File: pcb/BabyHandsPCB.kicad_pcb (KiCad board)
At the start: 2 copper layers, 44 parts

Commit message: Route matrix
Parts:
- removed Dn: D_Small, kbd:D3_TH_SMD
- added D10: D_Small, kbd:D3_TH_SMD, F.Cu at (108.0, 192.1)
- MX1, MX10, MX11, MX12, MX13, MX14, MX15, MX16, MX17, MX19, MX2, MX20, MX21, MX3, MX4, MX5, MX6, MX7, MX8, MX9: footprint kbd:MX_ALPS_PG1350_noLed -> kbd:CherryMX_Choc_Hotswap
- MX18, MX22: footprint kbd:MX_ALPS_PG1350_noLed_1.75u -> kbd:CherryMX_Choc_Hotswap_1.5u
- moved MX10 125.7 mm to (117.7, 194.7)
- moved D18 125.0 mm to (166.7, 202.4), turned to 320 degrees
- moved D22 124.4 mm to (180.4, 213.2), turned to 320 degrees
- moved MX18 123.9 mm to (173.8, 193.7), turned to 320 degrees
- moved MX22 123.2 mm to (188.1, 205.6), turned to 320 degrees
- moved MX14 122.7 mm to (145.3, 196.1)
- moved MX17 121.7 mm to (123.0, 167.5)
- moved D14 121.2 mm to (135.8, 190.6)
- moved D17 121.1 mm to (112.7, 167.5)
- moved MX21 118.1 mm to (145.3, 167.5)
- moved MX16 117.8 mm to (123.0, 145.3)
- moved D21 117.4 mm to (134.9, 167.5)
- moved D16 117.3 mm to (112.7, 145.3)
- moved MX20 114.3 mm to (145.3, 145.3)
- moved MX15 114.0 mm to (123.0, 123.0)
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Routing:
- net Col5: track 0.00 -> 243.6 mm, vias 0 -> 9
- net Col3: track 0.00 -> 240.0 mm, vias 0 -> 9
- net Col2: track 0.00 -> 223.0 mm, vias 0 -> 9
- net Col4: track 0.00 -> 212.8 mm, vias 0 -> 8
- net Row1: track 0.00 -> 186.1 mm
- net Row2: track 0.00 -> 183.3 mm
- net Col1: track 0.00 -> 142.9 mm, vias 0 -> 7
- net Row0: track 44.7 -> 184.2 mm
- net Col0: track 0.00 -> 134.2 mm, vias 0 -> 7
- net Row3: track 0.00 -> 99.3 mm
- net Net-(D2-Pad2): track 0.00 -> 55.3 mm, vias 0 -> 2
- net Net-(D14-Pad2): track 0.00 -> 53.6 mm, vias 0 -> 2
- net Net-(D17-Pad2): track 0.00 -> 51.5 mm, vias 0 -> 2
- net Net-(D11-Pad2): track 0.00 -> 51.0 mm, vias 0 -> 2
- net Net-(D21-Pad2): track 0.00 -> 49.8 mm, vias 0 -> 2
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
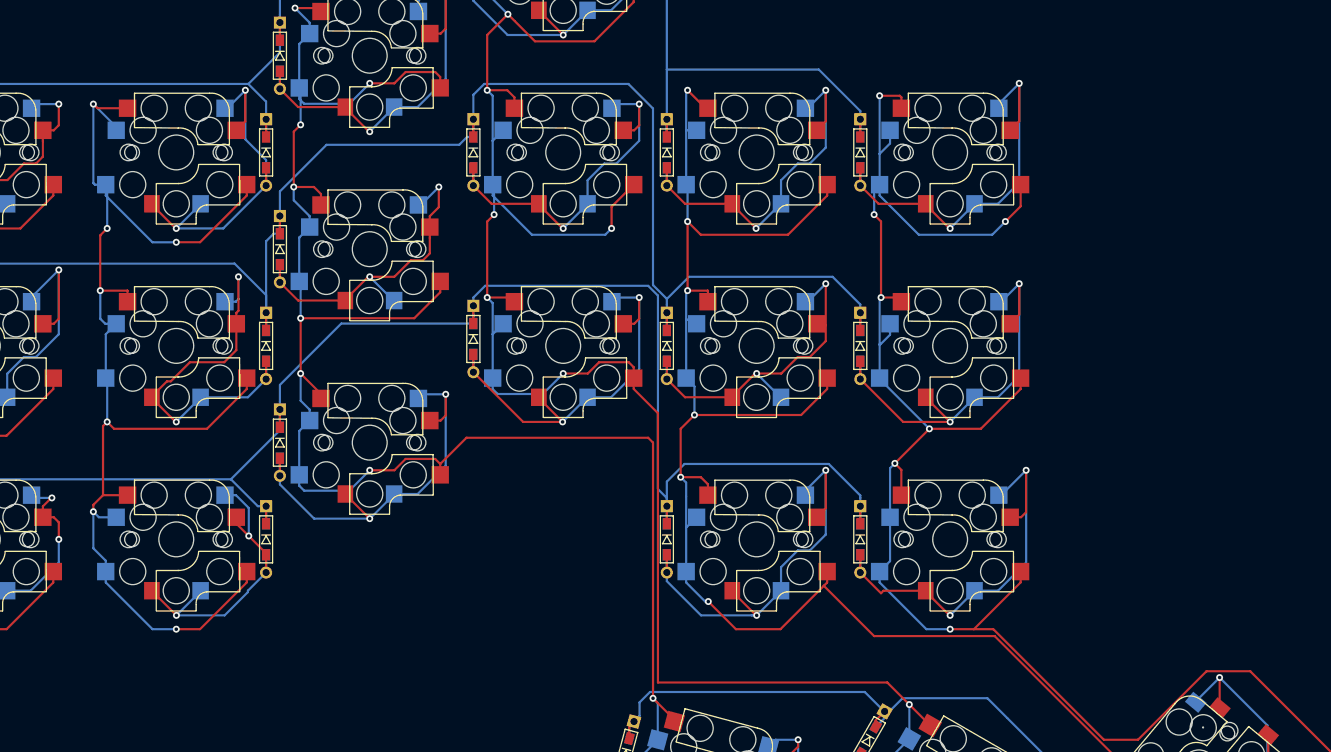
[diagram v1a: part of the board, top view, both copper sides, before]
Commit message: Add pro micro
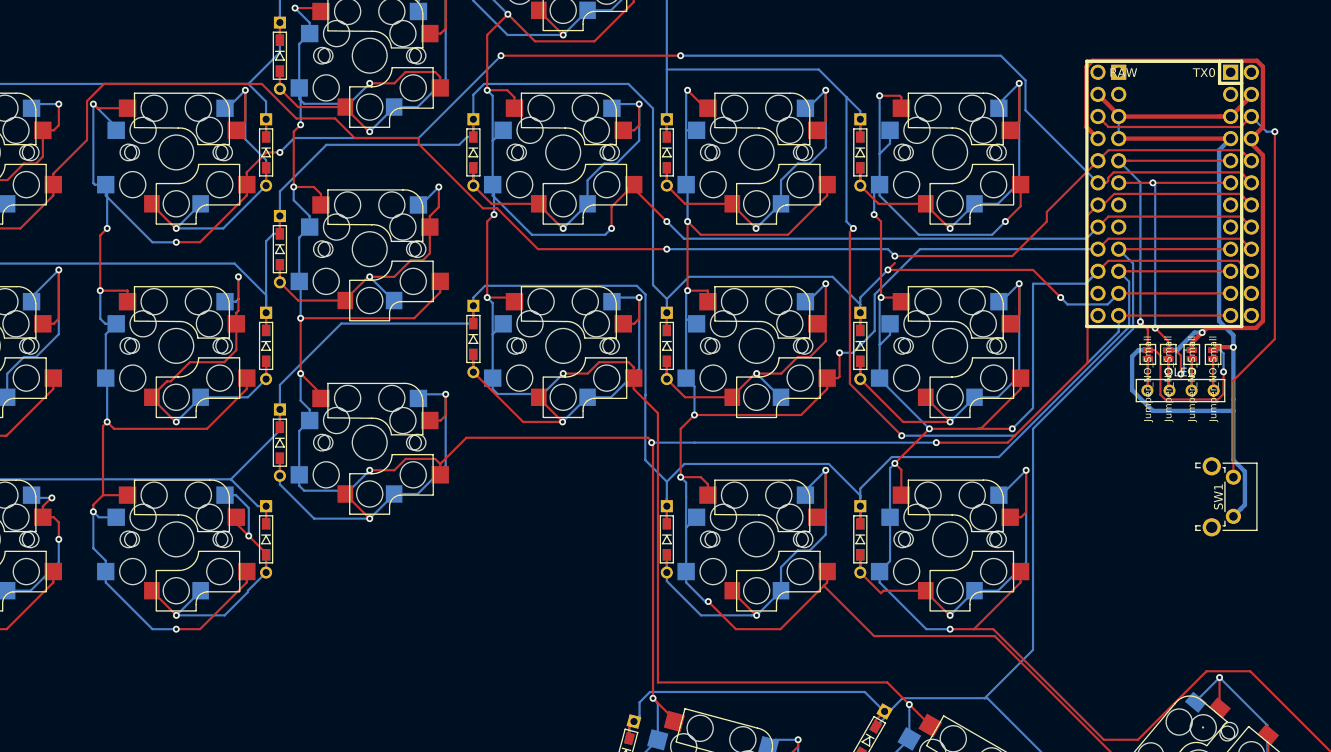
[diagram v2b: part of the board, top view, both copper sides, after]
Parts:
- added J1: Conn_01x04, kbd:OLED, F.Cu at (167.9, 150.4)
- added JP1: Jumper_NO_Small, kbd:Jumper, F.Cu at (175.5, 146.2)
- added JP2: Jumper_NO_Small, kbd:Jumper, F.Cu at (173.0, 146.2)
- added JP3: Jumper_NO_Small, kbd:Jumper, F.Cu at (170.3, 146.2)
- added JP4: Jumper_NO_Small, kbd:Jumper, F.Cu at (168.0, 146.2)
- added JP5: Jumper_NO_Small, kbd:Jumper, B.Cu at (175.5, 146.2)
- added JP6: Jumper_NO_Small, kbd:Jumper, B.Cu at (173.0, 146.2)
- added JP7: Jumper_NO_Small, kbd:Jumper, B.Cu at (170.3, 146.2)
- added JP8: Jumper_NO_Small, kbd:Jumper, B.Cu at (168.0, 146.2)
- added SW1: SW_PUSH, Button_Switch_THT:SW_Tactile_SPST_Angled_PTS645Vx31-2LFS, F.Cu at (177.8, 160.3)
- added U1: ProMicro, Keebio-Parts:ArduinoProMicro-BackSide, B.Cu at (169.9, 127.8)
- added U2: ProMicro, Keebio-Parts:ArduinoProMicro-BackSide, F.Cu at (172.2, 127.8)
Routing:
- net Col0: track 134.2 -> 294.8 mm, vias 7 -> 9
- net Col1: track 142.9 -> 274.5 mm, vias 7 -> 10
- net GND: track 0.00 -> 102.1 mm, vias 0 -> 1
- net Col2: track 223.0 -> 314.2 mm, vias 9 -> 11
- net Row0: track 184.2 -> 270.6 mm, vias 0 -> 2
- net Col3: track 240.0 -> 315.3 mm, vias 9 -> 10
- net VCC: track 0.00 -> 75.0 mm, vias 0 -> 1
- net Row3: track 99.3 -> 171.5 mm
- net RST: track 0.00 -> 63.7 mm, vias 0 -> 1
- net Col4: track 212.8 -> 272.7 mm, vias 8 -> 9
- net Row2: track 183.3 -> 240.0 mm
- net SDA: track 0.00 -> 56.0 mm, vias 0 -> 2
- net Col5: track 243.6 -> 294.0 mm, vias 9 -> 10
- net Row1: track 186.1 -> 234.1 mm, vias 0 -> 2
- net SCL: track 0.00 -> 40.5 mm, vias 0 -> 3
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
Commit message: Add outline
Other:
- board outline added: 186.5 x 136.7 mm
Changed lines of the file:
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@@
   (general
     (thickness 1.6)
-    (drawings 0)
+    (drawings 14)
     (tracks 1231)
     (zones 0)
@@
     )
   )
+  (gr_line (start 65.866 99.288) (end 65.866 110.288) (layer Edge.Cuts) (width 0.05))
+  (gr_line (start 88.316 99.288) (end 65.866 99.288) (layer Edge.Cuts) (width 0.05))
+  (gr_line (start 88.316 88.088) (end 88.316 99.288) (layer Edge.Cuts) (width 0.05))
+  (gr_line (start 114.166 88.088) (end 88.316 88.088) (layer Edge.Cuts) (width 0.05))
+  (gr_line (start 114.166 110.938) (end 114.166 88.088) (layer Edge.Cuts) (width 0.05))
+  (gr_line (start 185.166 110.938) (end 114.166 110.938) (layer Edge.Cuts) (width 0.05))
+  (gr_line (start 21.316 179.788) (end 21.316 110.288) (layer Edge.Cuts) (width 0.05))
+  (gr_line (start 67.416 179.788) (end 21.316 179.788) (layer Edge.Cuts) (width 0.05))
+  (gr_line (start 103.516 204.838) (end 67.416 179.788) (layer Edge.Cuts) (width 0.05))
+  (gr_line (start 187.066 224.788) (end 103.516 204.838) (layer Edge.Cuts) (width 0.05))
+  (gr_line (start 207.816 200.588) (end 187.066 224.788) (layer Edge.Cuts) (width 0.05))
+  (gr_line (start 185.116 182.088) (end 207.816 200.588) (layer Edge.Cuts) (width 0.05))
+  (gr_line (start 185.166 110.938) (end 185.116 182.088) (layer Edge.Cuts) (width 0.05))
+  (gr_line (start 21.316 110.288) (end 65.866 110.288) (layer Edge.Cuts) (width 0.05))
   (segment (start 25.9025 128.93125) (end 31.33125 128.93125) (width 0.25) (layer F.Cu) (net 1))
   (segment (start 23.8125 126.84125) (end 25.9025 128.93125) (width 0.25) (layer F.Cu) (net 1))

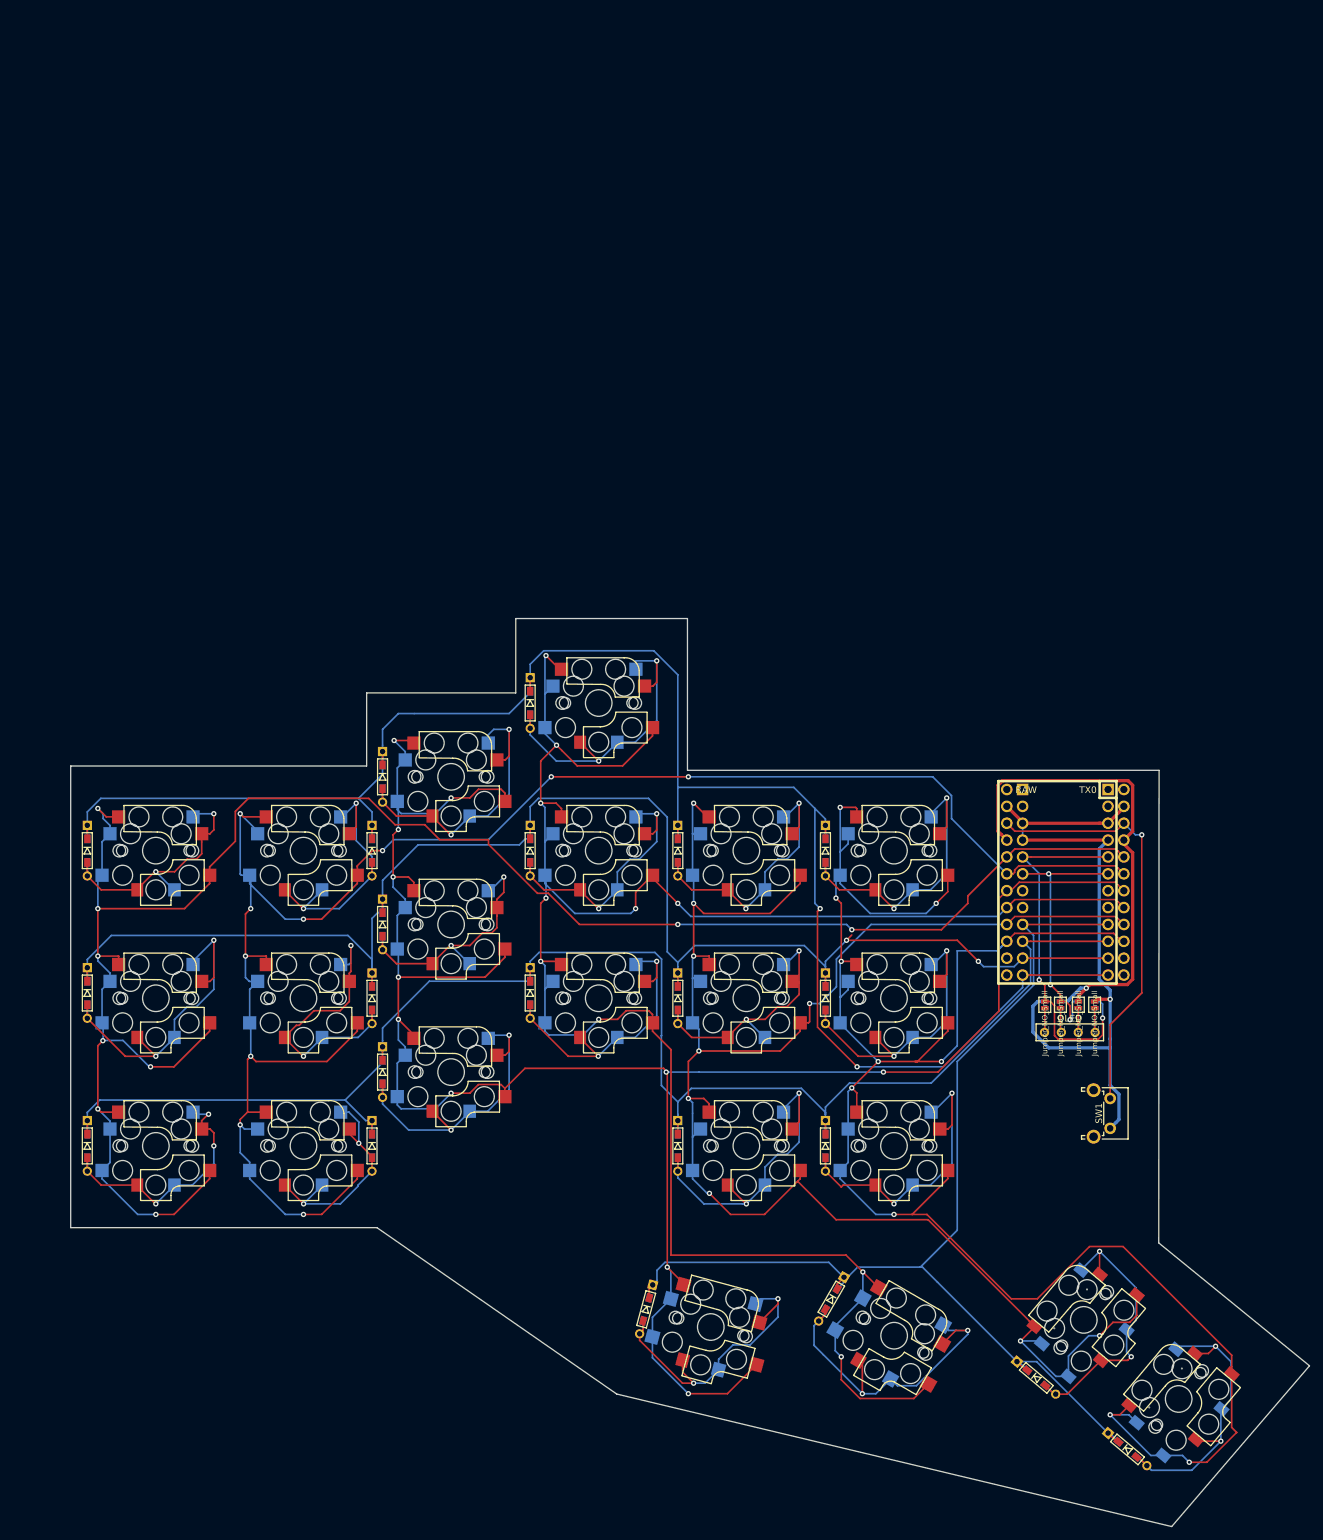
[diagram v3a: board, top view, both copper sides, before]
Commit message: Round edges
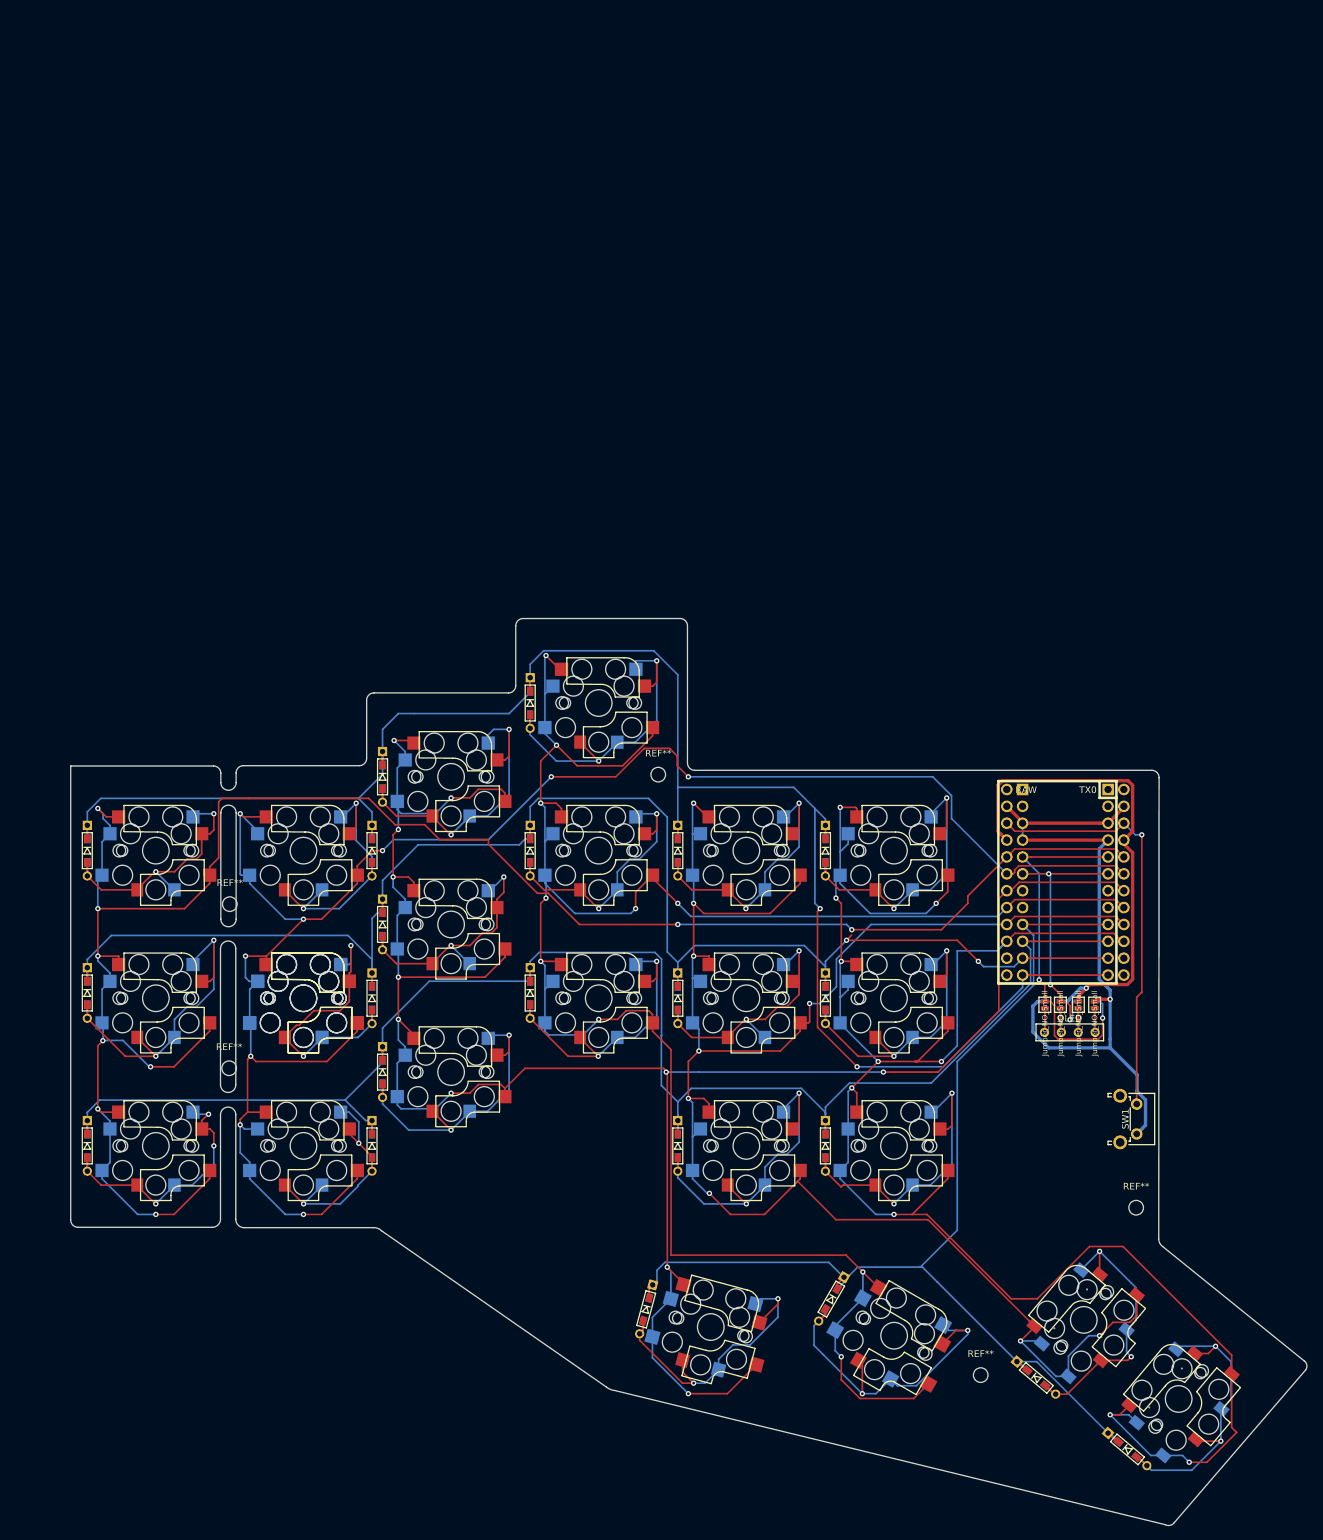
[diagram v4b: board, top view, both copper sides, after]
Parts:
- added MX5: MX-NoLED, kbd:CherryMX_Choc_Hotswap, F.Cu at (56.4, 145.3)
- added REF**: MountingHole_2.2mm_M2, MountingHole:MountingHole_2.2mm_M2, F.Cu at (109.8, 111.6)
- added REF**: MountingHole_2.2mm_M2, MountingHole:MountingHole_2.2mm_M2, F.Cu at (181.7, 176.8)
- added REF**: MountingHole_2.2mm_M2, MountingHole:MountingHole_2.2mm_M2, F.Cu at (158.3, 202.0)
- added REF**: MountingHole_2.2mm_M2, MountingHole:MountingHole_2.2mm_M2, F.Cu at (45.2, 155.8)
- added REF**: MountingHole_2.2mm_M2, MountingHole:MountingHole_2.2mm_M2, F.Cu at (45.3, 131.1)
- moved SW1 4.09 mm to (181.8, 161.2)
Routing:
- net GND: track 102.1 -> 104.7 mm
- net Col0: track 294.8 -> 297.2 mm
- net RST: track 63.7 -> 63.0 mm
- net Col1: vias 10 -> 9
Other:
- board size 186.5 x 136.7 mm -> 186.1 x 136.5 mm
